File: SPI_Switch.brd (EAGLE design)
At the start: 100 x 80 mm, 7 parts

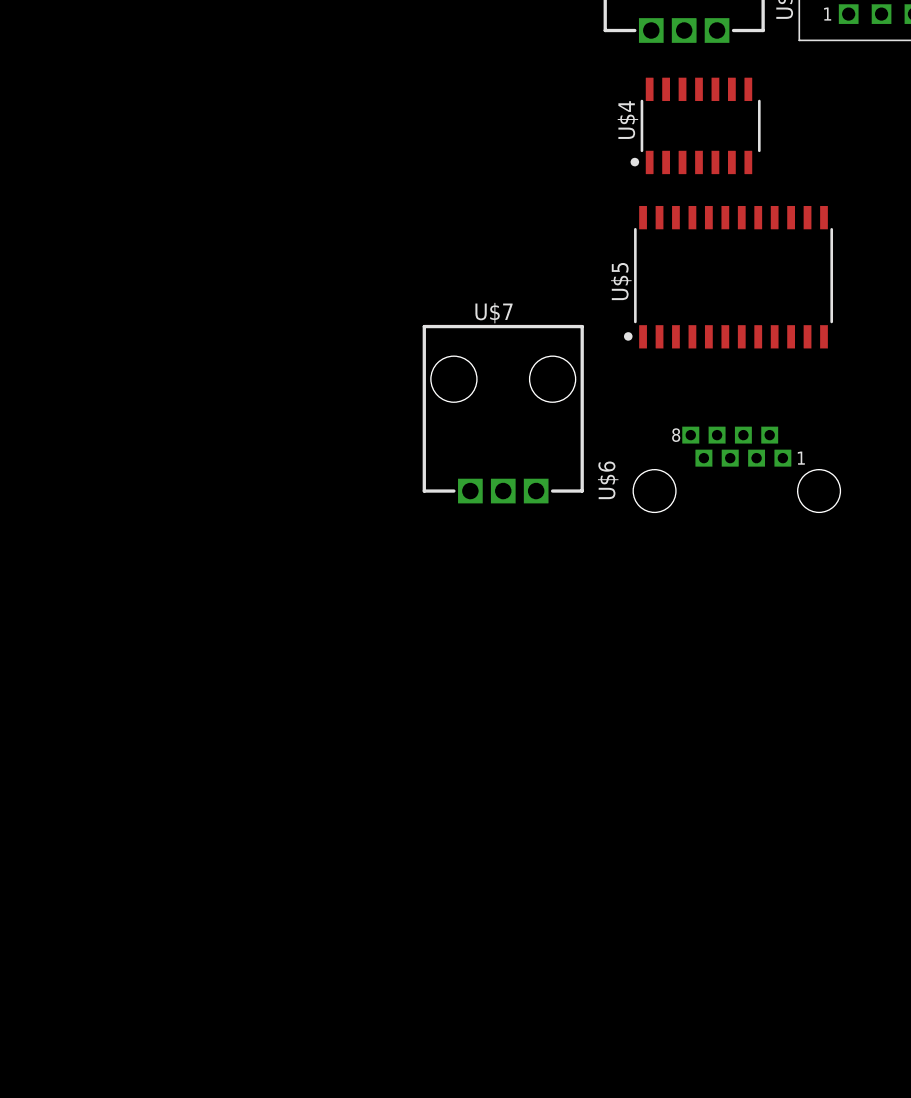
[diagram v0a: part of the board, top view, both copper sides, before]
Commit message: updated library parts for easier schematic
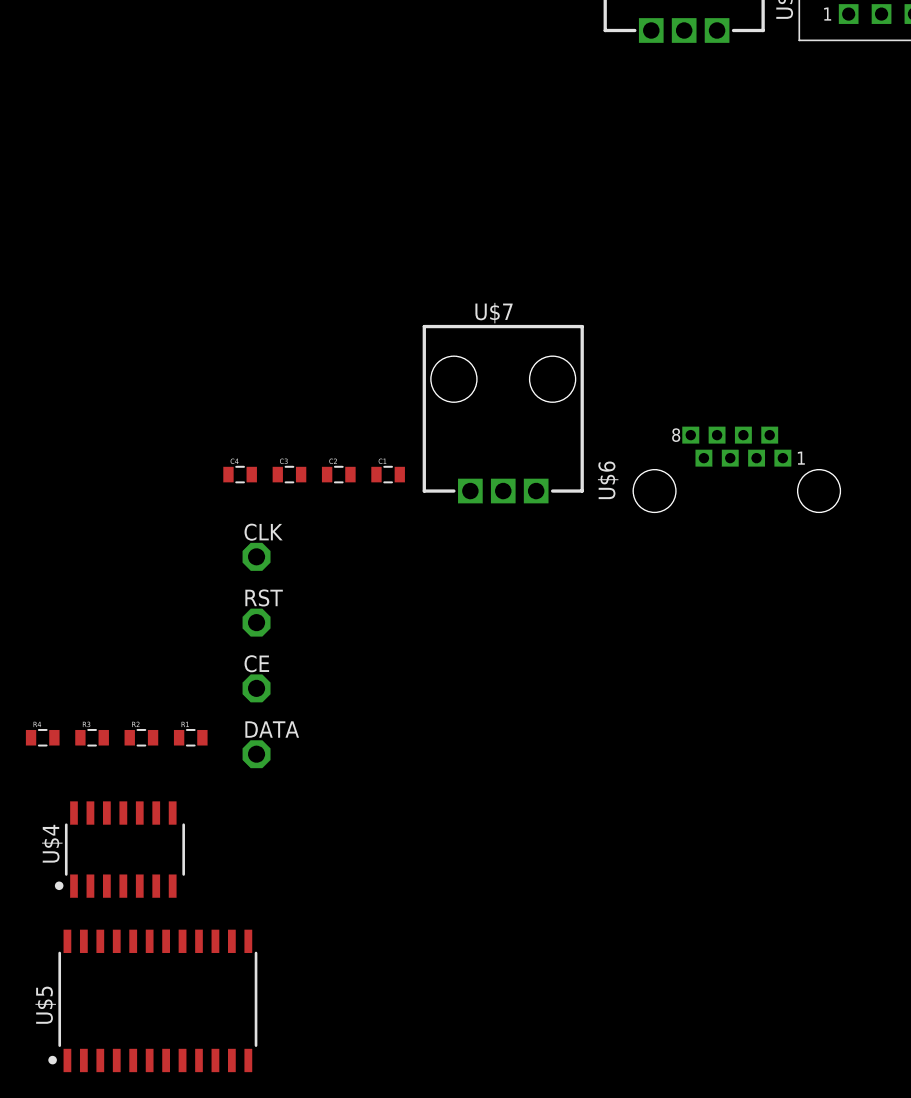
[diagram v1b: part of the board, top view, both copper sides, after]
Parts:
- added C1: 220uF electrolytic, SparkFun-Passives:0805
- added C2: 47uF, SparkFun-Passives:0805
- added C3: 10uF, SparkFun-Passives:0805
- added C4: 1uF, SparkFun-Passives:0805
- added CE, CLK, DATA, RST: PTR1PAD1-13, testpad:P1-13
- added R1, R2, R3, R4: 0, SparkFun-Passives:0805
- moved U$4 71.4 mm to (-54.6, -82.5)
- moved U$5 71.4 mm to (-57.1, -99.1)
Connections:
- removed net N$1: U$3.P$1, U$7.P$1
- removed net N$2: U$3.P$2, U$7.P$2
- removed net N$3: U$3.P$3, U$7.P$3
- new net +24V: C1.1, U$3.P$1, U$7.P$1
- new net +5V: C2.1, C3.1, C4.1, U$3.P$2, U$5.11, U$5.23, U$7.P$2
- new net CE: CE.TP, R4.1, U$1.P$6, U$4.12
- new net CE_POST: R4.2, U$4.11
- new net CLK: CLK.TP, R2.1, U$1.P$2, U$4.5, U$5.13
- new net CLK_POST: R2.2, U$4.6
- new net DATA_IN: DATA.TP, U$1.P$8, U$5.14
- new net DATA_OUT: R1.1, U$4.2, U$5.12
- new net DATA_OUT_POST: R1.2, U$4.3
- new net GND: C1.2, C2.2, C3.2, C4.2, U$1.P$1, U$1.P$3, U$1.P$5, U$1.P$7, U$3.P$3, U$5.17, U$5.18, U$5.19, U$5.20, U$5.5, U$5.6, U$5.7, U$5.8, U$7.P$3
- new net RST: R3.1, RST.TP, U$1.P$4, U$4.9, U$5.24
- new net RST_POST: R3.2, U$4.8
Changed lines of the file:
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@@
 <element name="U$2" library="SPI_Switch" package="8516-4500PL" value="8516-4500PL" x="6.35" y="-13.97"/>
 <element name="U$3" library="SPI_Switch" package="0705510037" value="0705510037" x="-8.89" y="-15.24"/>
-<element name="U$4" library="SPI_Switch" package="SN74ABT126" value="SN74ABT126" x="-10.16" y="-26.67"/>
-<element name="U$5" library="SPI_Switch" package="TLE7230G" value="TLE7230G" x="-12.7" y="-43.18"/>
 <element name="U$6" library="SPI_Switch" package="1-406525-1" value="1-406525-1" x="1.27" y="-48.26"/>
 <element name="U$7" library="SPI_Switch" package="0705510037" value="0705510037" x="-22.86" y="-50.8"/>
+<element name="C1" library="SparkFun-Passives" package="0805" value="220uF electrolytic" x="-29.21" y="-49.53"/>
+<element name="C2" library="SparkFun-Passives" package="0805" value="47uF" x="-33.02" y="-49.53"/>
+<element name="C3" library="SparkFun-Passives" package="0805" value="10uF" x="-36.83" y="-49.53"/>
+<element name="C4" library="SparkFun-Passives" package="0805" value="1uF" x="-40.64" y="-49.53"/>
+<element name="CLK" library="testpad" package="P1-13" value="PTR1PAD1-13" x="-39.37" y="-55.88">
+<attribute name="TP_SIGNAL_NAME" value="" x="-39.37" y="-55.88" size="1.778" layer="27" display="off"/>
+</element>
+<element name="RST" library="testpad" package="P1-13" value="PTR1PAD1-13" x="-39.37" y="-60.96">
+<attribute name="TP_SIGNAL_NAME" value="" x="-39.37" y="-60.96" size="1.778" layer="27" display="off"/>
+</element>
+<element name="CE" library="testpad" package="P1-13" value="PTR1PAD1-13" x="-39.37" y="-66.04">
+<attribute name="TP_SIGNAL_NAME" value="" x="-39.37" y="-66.04" size="1.778" layer="27" display="off"/>
+</element>
+<element name="DATA" library="testpad" package="P1-13" value="PTR1PAD1-13" x="-39.37" y="-71.12">
+<attribute name="TP_SIGNAL_NAME" value="" x="-39.37" y="-71.12" size="1.778" layer="27" display="off"/>
+</element>
+<element name="R1" library="SparkFun-Passives" package="0805" value="0" x="-44.45" y="-69.85"/>
+<element name="R2" library="SparkFun-Passives" package="0805" value="0" x="-48.26" y="-69.85"/>
+<element name="R3" library="SparkFun-Passives" package="0805" value="0" x="-52.07" y="-69.85"/>
+<element name="R4" library="SparkFun-Passives" package="0805" value="0" x="-55.88" y="-69.85"/>
+<element name="U$4" library="SPI_Switch" package="SN74ABT126" value="SN74ABT126" x="-54.61" y="-82.55"/>
+<element name="U$5" library="SPI_Switch" package="TLE7230G" value="TLE7230G" x="-57.15" y="-99.06"/>
 </elements>
 <signals>
-<signal name="N$1">
+<signal name="GND">
+<contactref element="U$3" pad="P$3"/>
+<contactref element="U$7" pad="P$3"/>
+<contactref element="C1" pad="2"/>
+<contactref element="C2" pad="2"/>
+<contactref element="C4" pad="2"/>
+<contactref element="C3" pad="2"/>
+<contactref element="U$1" pad="P$1"/>
+<contactref element="U$1" pad="P$7"/>
+<contactref element="U$1" pad="P$5"/>
+<contactref element="U$1" pad="P$3"/>
+<contactref element="U$5" pad="5"/>
+<contactref element="U$5" pad="20"/>
+<contactref element="U$5" pad="19"/>
+<contactref element="U$5" pad="18"/>
+<contactref element="U$5" pad="17"/>
+<contactref element="U$5" pad="8"/>
+<contactref element="U$5" pad="7"/>
+<contactref element="U$5" pad="6"/>
+<wire x1="-47.625" y1="-94.77" x2="-48.895" y2="-94.77" width="0" layer="19" extent="1-1"/>
+<wire x1="-46.355" y1="-94.77" x2="-47.625" y2="-94.77" width="0" layer="19" extent="1-1"/>
+<wire x1="-45.085" y1="-94.77" x2="-46.355" y2="-94.77" width="0" layer="19" extent="1-1"/>
+<wire x1="-48.895" y1="-85.57" x2="-48.895" y2="-94.77" width="0" layer="19" extent="1-1"/>
+<wire x1="-47.625" y1="-85.57" x2="-48.895" y2="-85.57" width="0" layer="19" extent="1-1"/>
+<wire x1="-46.355" y1="-85.57" x2="-47.625" y2="-85.57" width="0" layer="19" extent="1-1"/>
+<wire x1="-45.085" y1="-85.57" x2="-46.355" y2="-85.57" width="0" layer="19" extent="1-1"/>
+<wire x1="-39.74" y1="-49.53" x2="-45.085" y2="-85.57" width="0" layer="19" extent="1-1"/>
+<wire x1="-35.93" y1="-49.53" x2="-39.74" y2="-49.53" width="0" layer="19" extent="1-1"/>
+<wire x1="-32.12" y1="-49.53" x2="-35.93" y2="-49.53" width="0" layer="19" extent="1-1"/>
+<wire x1="-28.31" y1="-49.53" x2="-32.12" y2="-49.53" width="0" layer="19" extent="1-1"/>
+<wire x1="-17.78" y1="-50.8" x2="-28.31" y2="-49.53" width="0" layer="19" extent="1-1"/>
+<wire x1="-3.81" y1="-15.24" x2="-17.78" y2="-50.8" width="0" layer="19" extent="1-1"/>
+<wire x1="9.144" y1="-3.81" x2="-3.81" y2="-15.24" width="0" layer="19" extent="1-1"/>
+<wire x1="11.176" y1="-3.81" x2="9.144" y2="-3.81" width="0" layer="19" extent="1-1"/>
+<wire x1="13.208" y1="-3.81" x2="11.176" y2="-3.81" width="0" layer="19" extent="1-1"/>
+<wire x1="15.24" y1="-3.81" x2="13.208" y2="-3.81" width="0" layer="19" extent="1-1"/>
+</signal>
+<signal name="+24V">
 <contactref element="U$3" pad="P$1"/>
 <contactref element="U$7" pad="P$1"/>
+<contactref element="C1" pad="1"/>
+<wire x1="-22.86" y1="-50.8" x2="-30.11" y2="-49.53" width="0" layer="19" extent="1-1"/>
 <wire x1="-8.89" y1="-15.24" x2="-22.86" y2="-50.8" width="0" layer="19" extent="1-1"/>
 </signal>
-<signal name="N$2">
+<signal name="+5V">
 <contactref element="U$3" pad="P$2"/>
 <contactref element="U$7" pad="P$2"/>
+<contactref element="C2" pad="1"/>
+<contactref element="C4" pad="1"/>
+<contactref element="C3" pad="1"/>
+<contactref element="U$5" pad="23"/>
+<contactref element="U$5" pad="11"/>
+<wire x1="-41.275" y1="-94.77" x2="-52.705" y2="-85.57" width="0" layer="19" extent="1-1"/>
+<wire x1="-41.54" y1="-49.53" x2="-52.705" y2="-85.57" width="0" layer="19" extent="1-1"/>
+<wire x1="-37.73" y1="-49.53" x2="-41.54" y2="-49.53" width="0" layer="19" extent="1-1"/>
+<wire x1="-33.92" y1="-49.53" x2="-37.73" y2="-49.53" width="0" layer="19" extent="1-1"/>
+<wire x1="-20.32" y1="-50.8" x2="-33.92" y2="-49.53" width="0" layer="19" extent="1-1"/>
 <wire x1="-6.35" y1="-15.24" x2="-20.32" y2="-50.8" width="0" layer="19" extent="1-1"/>
 </signal>
-<signal name="N$3">
-<contactref element="U$3" pad="P$3"/>
-<contactref element="U$7" pad="P$3"/>
-<wire x1="-3.81" y1="-15.24" x2="-17.78" y2="-50.8" width="0" layer="19" extent="1-1"/>
+<signal name="RST">
+<contactref element="U$1" pad="P$4"/>
+<contactref element="RST" pad="TP"/>
+<contactref element="U$5" pad="24"/>
+<contactref element="U$4" pad="9"/>
+<contactref element="R3" pad="1"/>
+<wire x1="-47.117" y1="-75.664" x2="-53.975" y2="-85.57" width="0" layer="19" extent="1-1"/>
+<wire x1="-52.97" y1="-69.85" x2="-47.117" y2="-75.664" width="0" layer="19" extent="1-1"/>
+<wire x1="-39.37" y1="-60.96" x2="-52.97" y2="-69.85" width="0" layer="19" extent="1-1"/>
+<wire x1="12.192" y1="-2.032" x2="-39.37" y2="-60.96" width="0" layer="19" extent="1-1"/>
+</signal>
+<signal name="CE">
+<contactref element="U$1" pad="P$6"/>
+<contactref element="CE" pad="TP"/>
+<contactref element="U$4" pad="12"/>
+<contactref element="R4" pad="1"/>
+<wire x1="-56.78" y1="-69.85" x2="-50.927" y2="-75.664" width="0" layer="19" extent="1-1"/>
+<wire x1="-39.37" y1="-66.04" x2="-50.927" y2="-75.664" width="0" layer="19" extent="1-1"/>
+<wire x1="10.16" y1="-2.032" x2="-39.37" y2="-66.04" width="0" layer="19" extent="1-1"/>
+</signal>
+<signal name="DATA_IN">
+<contactref element="U$1" pad="P$8"/>
+<contactref element="DATA" pad="TP"/>
+<contactref element="U$5" pad="14"/>
+<wire x1="-39.37" y1="-71.12" x2="-41.275" y2="-85.57" width="0" layer="19" extent="1-1"/>
+<wire x1="8.128" y1="-2.032" x2="-39.37" y2="-71.12" width="0" layer="19" extent="1-1"/>
+</signal>
+<signal name="CLK">
+<contactref element="U$1" pad="P$2"/>
+<contactref element="CLK" pad="TP"/>
+<contactref element="U$5" pad="13"/>
+<contactref element="U$4" pad="5"/>
+<contactref element="R2" pad="1"/>
+<wire x1="-40.005" y1="-85.57" x2="-48.387" y2="-81.308" width="0" layer="19" extent="1-1"/>
+<wire x1="-49.16" y1="-69.85" x2="-48.387" y2="-81.308" width="0" layer="19" extent="1-1"/>
+<wire x1="-39.37" y1="-55.88" x2="-49.16" y2="-69.85" width="0" layer="19" extent="1-1"/>
+<wire x1="14.224" y1="-2.032" x2="-39.37" y2="-55.88" width="0" layer="19" extent="1-1"/>
+</signal>
+<signal name="DATA_OUT">
+<contactref element="U$5" pad="12"/>
+<contactref element="U$4" pad="2"/>
+<contactref element="R1" pad="1"/>
+<wire x1="-52.197" y1="-81.308" x2="-40.005" y2="-94.77" width="0" layer="19" extent="1-1"/>
+<wire x1="-45.35" y1="-69.85" x2="-52.197" y2="-81.308" width="0" layer="19" extent="1-1"/>
+</signal>
+<signal name="DATA_OUT_POST">
+<contactref element="U$4" pad="3"/>
+<contactref element="R1" pad="2"/>
+<wire x1="-43.55" y1="-69.85" x2="-50.927" y2="-81.308" width="0" layer="19" extent="1-1"/>
+</signal>
+<signal name="CLK_POST">
+<contactref element="U$4" pad="6"/>
+<contactref element="R2" pad="2"/>
+<wire x1="-47.36" y1="-69.85" x2="-47.117" y2="-81.308" width="0" layer="19" extent="1-1"/>
+</signal>
+<signal name="RST_POST">
+<contactref element="U$4" pad="8"/>
+<contactref element="R3" pad="2"/>
+<wire x1="-51.17" y1="-69.85" x2="-45.847" y2="-75.664" width="0" layer="19" extent="1-1"/>
+</signal>
+<signal name="CE_POST">
+<contactref element="U$4" pad="11"/>
+<contactref element="R4" pad="2"/>
+<wire x1="-54.98" y1="-69.85" x2="-49.657" y2="-75.664" width="0" layer="19" extent="1-1"/>
 </signal>
 </signals>

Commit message: added stuff
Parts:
- added C5, C6: 10uF, SparkFun-Passives:0805
- added LED1, LED2, LED3, LED4, LED5, LED6, LED7: (no value), led:SMARTLED-TTW
- added R10, R11, R12, R6, R7, R8, R9: 1k, SparkFun-Passives:0805
- added R5: DNP, SparkFun-Passives:0805
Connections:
- new net CH1: U$2.P$3, U$2.P$4, U$5.21
- new net CH2: U$2.P$5, U$2.P$6, U$5.22
- new net CH3: U$2.P$7, U$2.P$8, U$5.3
- new net CH4: U$2.P$10, U$2.P$9, U$5.4
- new net CH5: U$2.P$11, U$2.P$12, U$5.9
- new net CH6: U$2.P$13, U$2.P$14, U$5.10
- new net CH7: U$2.P$16, U$5.15
- new net CH8: R5.1, U$5.16
- new net N$1: LED1.A@1, R7.2
- new net N$10: LED5.A@1, R10.2
- new net N$19: LED6.A@1, R11.2
- new net N$21: LED7.A@1, R12.2
- new net N$3: LED2.A@1, R6.2
- new net N$5: LED3.A@1, R8.2
- new net N$7: LED4.A@1, R9.2
- net +24V: now also U$2.P$1
- net +5V: now also C5.1, C6.1, U$4.1, U$4.10, U$4.13, U$4.14, U$4.4
- net CE_POST: now also U$6.P$6
- net CLK_POST: now also U$6.P$2
- net DATA_OUT_POST: now also U$6.P$8
- net GND: now also C5.2, C6.2, R5.2, U$2.P$15, U$4.7, U$6.P$1, U$6.P$3, U$6.P$5, U$6.P$7
- net RST_POST: now also U$6.P$4

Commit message: finished first take
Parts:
- added Q1, Q2, Q3, Q4, Q5, Q6, Q7: (no value), SparkFun-DiscreteSemi:SOT23
- LED1, LED2, LED3, LED4, LED5, LED6: value (none) -> GREEN
- LED7: value (none) -> RED
- moved R12 32.0 mm to (-81.3, -165.1)
- moved R11 26.9 mm to (-81.3, -153.7)
- moved LED7 25.7 mm to (-83.8, -161.3)
- moved R10 21.9 mm to (-81.3, -142.2)
- moved LED6 20.7 mm to (-83.8, -149.9)
- moved R9 16.9 mm to (-81.3, -130.8)
- moved LED5 15.7 mm to (-83.8, -138.4)
- moved R8 12.0 mm to (-81.3, -119.4)
- moved LED4 10.9 mm to (-83.8, -127.0)
- moved R6 7.41 mm to (-81.3, -108.0)
- moved LED3 6.35 mm to (-83.8, -115.6)
- moved LED2 3.81 mm to (-83.8, -104.1)
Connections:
- new net N$10: LED5.C@1, Q5.3
- new net N$12: LED6.C@1, Q6.3
- new net N$14: LED7.C@1, Q7.3
- new net N$2: LED1.C@1, Q1.3
- new net N$4: LED2.C@1, Q2.3
- new net N$6: LED3.C@1, Q3.3
- new net N$8: LED4.C@1, Q4.3
- net +24V: now also R10.1, R11.1, R12.1, R6.1, R7.1, R8.1, R9.1
- net CH1: now also Q1.1
- net CH2: now also Q2.1
- net CH3: now also Q3.1
- net CH4: now also Q4.1
- net CH5: now also Q5.1
- net CH6: now also Q6.1
- net CH7: now also Q7.1
- net GND: now also Q1.2, Q2.2, Q3.2, Q4.2, Q5.2, Q6.2, Q7.2

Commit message: adding daniel's changes
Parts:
- removed Q1, Q2, Q3, Q4, Q5, Q6, Q7: (no value), SparkFun-DiscreteSemi:SOT23
- removed U$2: 8516-4500PL, SPI_Switch:8516-4500PL
- added J1: 8516-4500PL, SPI_Switch:8516-4500PL
- R5: value DNP -> 1k
- moved R5 55.8 mm to (-83.8, -151.1)
- moved R12 14.9 mm to (-76.2, -151.1)
- moved LED7 14.5 mm to (-80.0, -147.3)
- moved LED6 13.5 mm to (-74.9, -139.7)
- moved R10 11.5 mm to (-69.8, -143.5)
- moved LED3 4.02 mm to (-80.0, -116.8)
- moved LED4 4.02 mm to (-80.0, -128.3)
- moved LED2 4.02 mm to (-80.0, -105.4)
- moved LED5 4.02 mm to (-80.0, -139.7)
- moved R11 2.84 mm to (-80.0, -151.1)
- moved R8 1.80 mm to (-80.0, -120.7)
- moved R9 1.80 mm to (-80.0, -132.1)
- moved R6 1.80 mm to (-80.0, -109.2)
- renumbered U$1 to J3, U$3 to J5, U$4 to U2, U$5 to U1, U$6 to J2, U$7 to J4
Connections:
- removed net N$10: LED5.C@1, Q5.3
- removed net N$12: LED6.C@1, Q6.3
- removed net N$14: LED7.C@1, Q7.3
- removed net N$2: LED1.C@1, Q1.3
- removed net N$4: LED2.C@1, Q2.3
- removed net N$6: LED3.C@1, Q3.3
- removed net N$8: LED4.C@1, Q4.3
- net +24V: now also J1.P$1, R5.1; no longer U$2.P$1
- net CH1: now also J1.P$3, LED1.C@1; no longer Q1.1, U$2.P$3, U$2.P$4
- net CH2: now also J1.P$5, LED2.C@1; no longer Q2.1, U$2.P$5, U$2.P$6
- net CH3: now also J1.P$7, LED3.C@1; no longer Q3.1, U$2.P$7, U$2.P$8
- net CH4: now also J1.P$9, LED4.C@1; no longer Q4.1, U$2.P$10, U$2.P$9
- net CH5: now also J1.P$11, LED5.C@1; no longer Q5.1, U$2.P$11, U$2.P$12
- net CH6: now also J1.P$13, LED6.C@1; no longer Q6.1, U$2.P$13, U$2.P$14
- net CH7: now also J1.P$16, LED7.C@1; no longer Q7.1, U$2.P$16
- net CH8: now also R5.2; no longer R5.1
- net GND: now also J1.P$15, U1.2; no longer Q1.2, Q2.2, Q3.2, Q4.2, Q5.2, Q6.2, Q7.2, R5.2, U$2.P$15
